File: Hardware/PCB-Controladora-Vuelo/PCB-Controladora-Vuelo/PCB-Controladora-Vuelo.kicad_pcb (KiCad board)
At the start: 2 copper layers, 40 x 90 mm, 14 parts, among them J1 Jumper Serial, J2 CONN, U1 MPU-5060, U2 ESP32-DEVKIT-V1, U3 Nrf24l01, U4 AMS1117-3.3

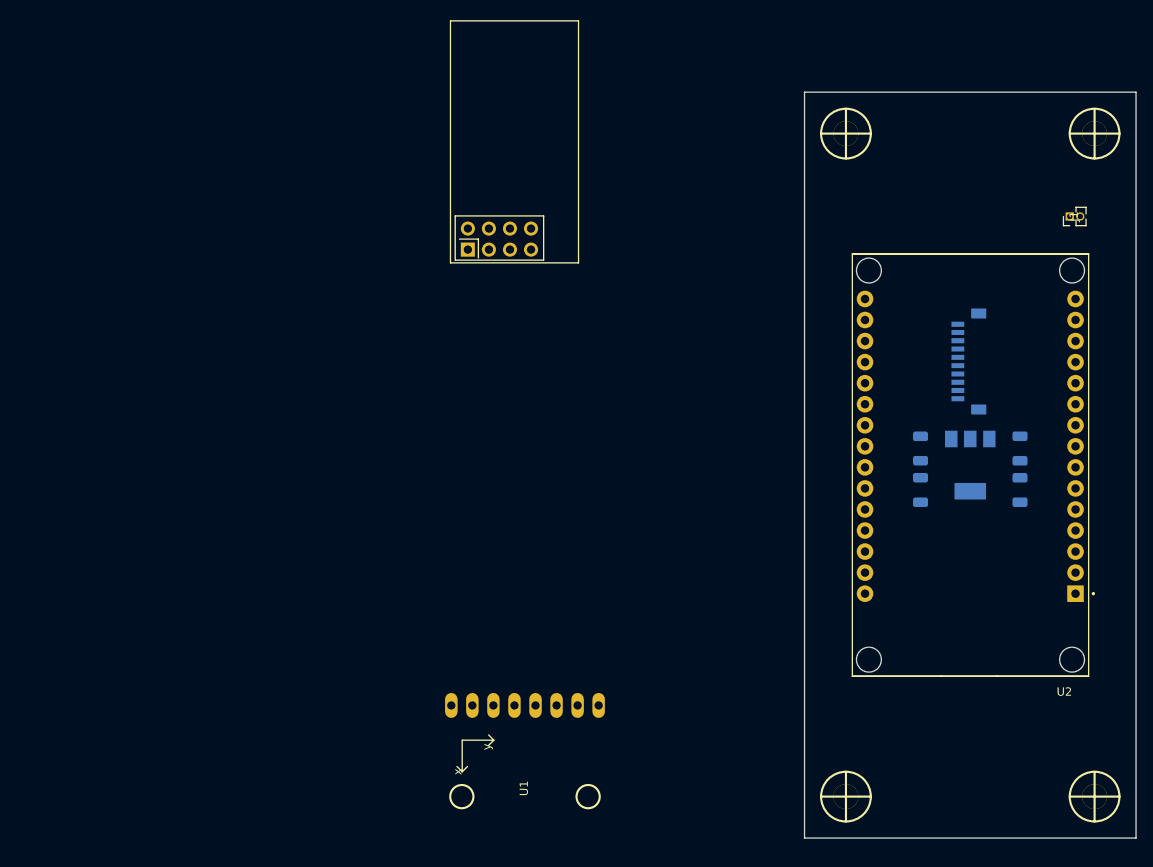
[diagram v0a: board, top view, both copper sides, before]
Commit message: subo cambios hechos en legui solucione mpu y lugar esp32 mal Footprints
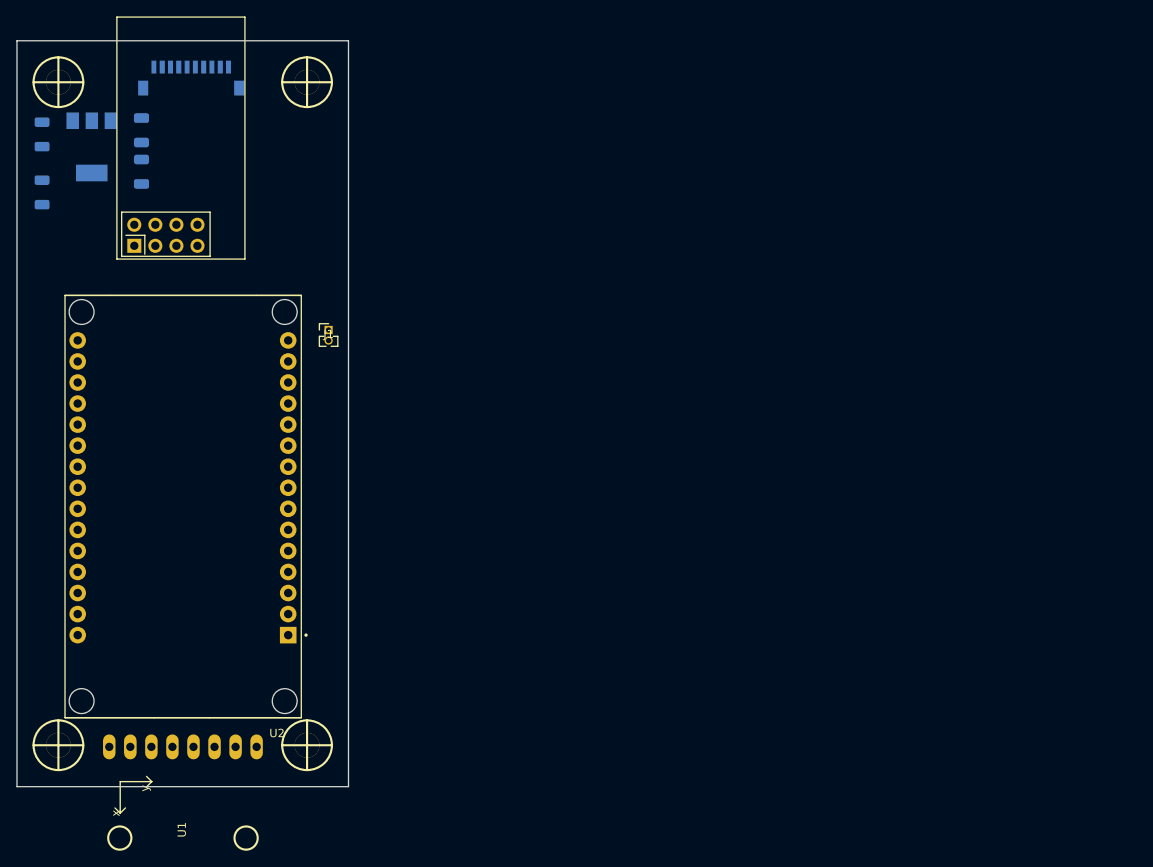
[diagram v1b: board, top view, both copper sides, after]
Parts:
- moved C1 112.7 mm to (129.0, 61.6)
- moved C3 112.7 mm to (129.0, 66.6)
- moved U4 112.7 mm to (123.0, 63.6)
- moved C7 112.6 mm to (117.0, 62.1)
- moved C5 111.9 mm to (117.0, 69.1)
- moved J2 100.6 mm to (135.0, 56.5), turned to 0 degrees
- moved H1 95.2 mm to (119.0, 55.8)
- moved H2 95.2 mm to (149.0, 55.8)
- moved H3 95.2 mm to (149.0, 135.8)
- moved H4 95.2 mm to (119.0, 135.8)
- moved U2 95.1 mm to (134.0, 107.0)
- moved J1 90.5 mm to (151.6, 85.7), turned to 0 degrees
- moved U1 41.6 mm to (142.9, 136.0)
- moved U3 40.3 mm to (128.1, 75.5)

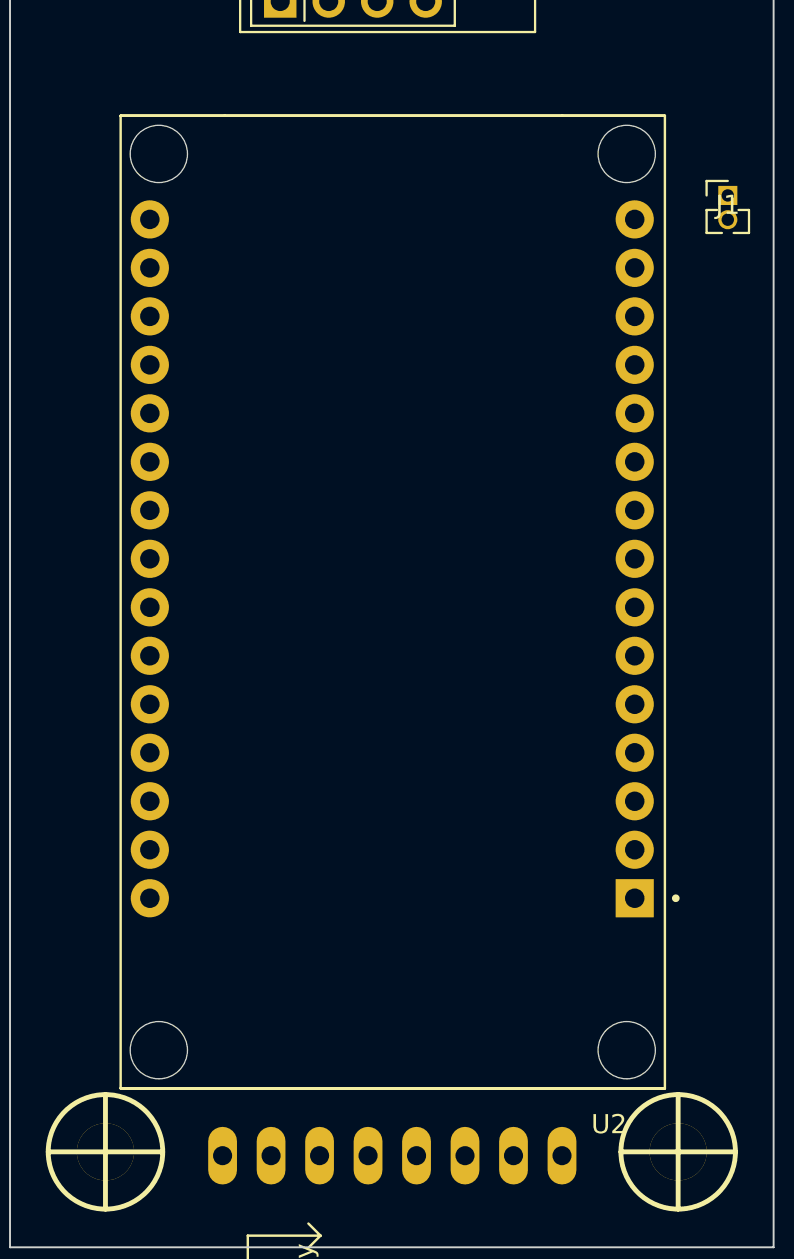
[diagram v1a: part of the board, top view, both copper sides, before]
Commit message: Realice cambios de huella ESP32 y Symbol
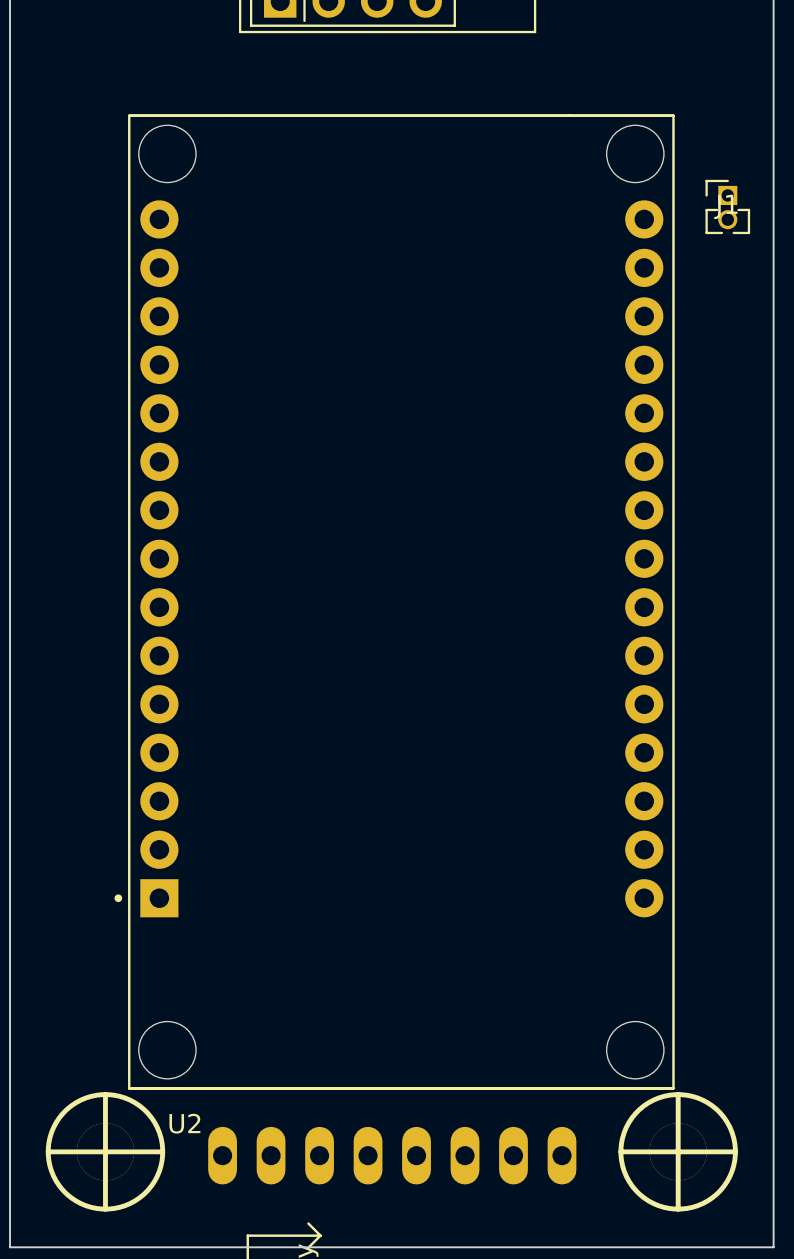
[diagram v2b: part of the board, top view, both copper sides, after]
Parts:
- C1: value 1uF -> 220uF
- C5: value 1uF -> 10uF
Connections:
- J2 pad 1: /NC -> unconnected-(J2-Pad1)
- J2 pad 3: /NC -> unconnected-(J2-Pad3)
- J2 pad 4: /NC -> unconnected-(J2-Pad4)
- J2 pad S1: /NC -> Net-(J2-SHIELD-PadS1)
- J2 pad S2: /NC -> Net-(J2-SHIELD-PadS1)
- U2 pad 1: unconnected-(U2-EN-Pad1) -> /Jumper_Serial
- U2 pad 10: /S2_MOTOR -> unconnected-(U2-D32-Pad10)
- U2 pad 11: /S3_MOTOR -> unconnected-(U2-D35-Pad11)
- U2 pad 12: /S4_MOTOR -> unconnected-(U2-D34-Pad12)
- U2 pad 14: GND -> unconnected-(U2-VP-Pad14)
- U2 pad 15: /Jumper_Serial -> unconnected-(U2-EN-Pad15)
- U2 pad 2: unconnected-(U2-VP-Pad2) -> GND
- U2 pad 4: unconnected-(U2-D34-Pad4) -> /S4_MOTOR
- U2 pad 5: unconnected-(U2-D35-Pad5) -> /S3_MOTOR
- U2 pad 6: unconnected-(U2-D32-Pad6) -> /S2_MOTOR
- U2 pad 7: unconnected-(U2-D33-Pad7) -> /S1_MOTOR
- U2 pad 9: /S1_MOTOR -> unconnected-(U2-D33-Pad9)

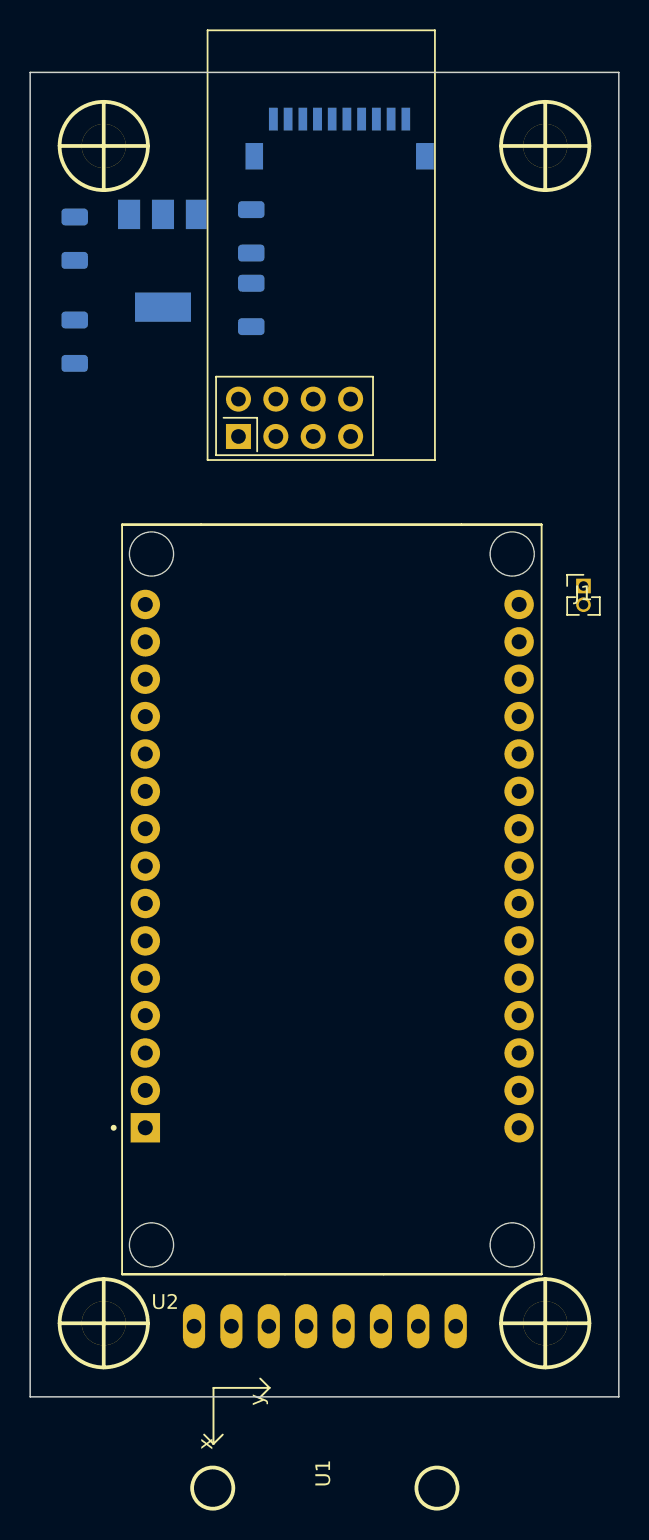
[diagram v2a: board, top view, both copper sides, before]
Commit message: muchos cambios leer saque todos los NC y coloque X ya que al poner etiquetas nc reconoce como que debe haber una conexion entre ellos y nqv tambien digamos que hice una buena 1ra parte de pcb, que se debe corregir y mirar todo mas a detalle , faltan definir unos pines para ver si es necesario para la primera prueba xD
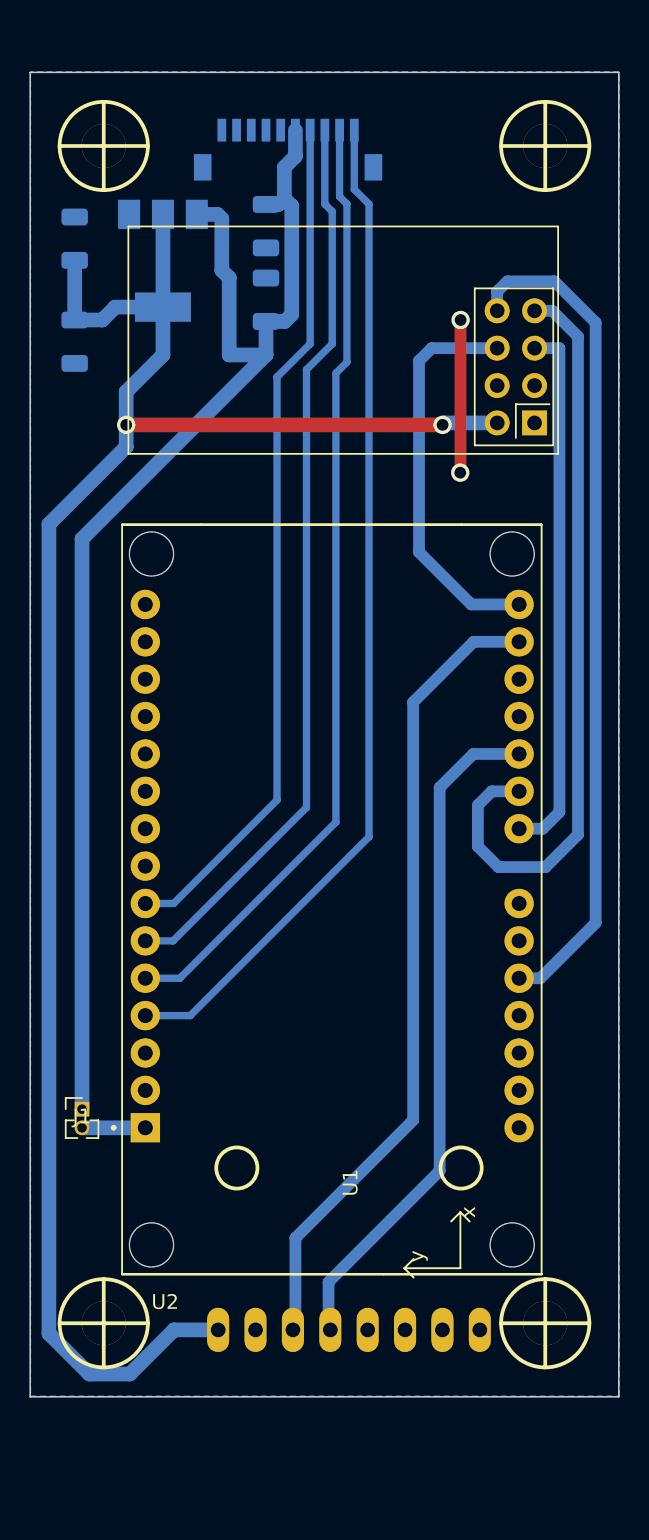
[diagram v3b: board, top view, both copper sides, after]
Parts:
- moved J1 49.2 mm to (117.5, 121.2)
- moved U3 20.1 mm to (148.2, 74.6), turned to 180 degrees
- moved U1 16.1 mm to (126.8, 136.2), turned to 90 degrees
- moved J2 3.58 mm to (131.5, 57.2)
- moved C1 1.06 mm to (130.0, 61.2)
- moved C3 1.06 mm to (130.0, 66.2)
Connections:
- J2 pad S1: Net-(J2-SHIELD-PadS1) -> unconnected-(J2-SHIELD-PadS1)
- J2 pad S2: Net-(J2-SHIELD-PadS1) -> unconnected-(J2-SHIELD-PadS1)
- U1 pad 5: /XDA_MPU6050 -> unconnected-(U1-XDA-Pad5)
- U1 pad 6: /XCL_MPU6050 -> unconnected-(U1-XCL-Pad6)
- U1 pad 7: /AD0_MPU6050 -> unconnected-(U1-ADO-Pad7)
- U1 pad 8: /INT_MPU6050 -> unconnected-(U1-INT-Pad8)
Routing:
- net +3V3: track 0.00 -> 128.8 mm, vias 0 -> 2
- net +5V: track 0.00 -> 88.9 mm
- net /S4_MOTOR: track 0.00 -> 68.7 mm
- net /S3_MOTOR: track 0.00 -> 64.9 mm
- net /S2_MOTOR: track 0.00 -> 61.7 mm
- net /S1_MOTOR: track 0.00 -> 58.3 mm
- net /IRQ_NRF24L01: track 0.00 -> 57.0 mm
- net /SCL_MPU6050: track 0.00 -> 54.9 mm
- net /MISO_NRF24L01: track 0.00 -> 51.8 mm
- net /SDA_MPU6050: track 0.00 -> 46.4 mm
- net /SCK_NRF24L01: track 0.00 -> 36.4 mm
- net /MOSI_NRF24L01: track 0.00 -> 26.9 mm
- net GND: track 0.00 -> 10.4 mm, vias 0 -> 2
- net /Jumper_Serial: track 0.00 -> 4.30 mm
- added copper zone on B.Cu, net GND

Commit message: Trabaje en el PCB corriegindo ordenes faltaria ver si se pueden agregar pines y corregir que no existan riesgo al momento de planchar o por un corto o abrirse el circuito
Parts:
- moved J2 3.23 mm to (134.0, 55.2)
- moved U3 2.55 mm to (145.7, 74.6)
- moved U1 2.47 mm to (125.0, 138.0)
- moved C1 2.38 mm to (132.1, 60.1)
- moved C3 2.38 mm to (132.1, 65.1)
- moved J1 0.62 mm to (118.1, 121.1)
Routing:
- net +3V3: track 128.8 -> 139.0 mm
- net GND: track 10.4 -> 19.1 mm
- net /S4_MOTOR: track 68.7 -> 72.7 mm
- net /S1_MOTOR: track 58.3 -> 62.2 mm
- net /S3_MOTOR: track 64.9 -> 68.7 mm
- net /S2_MOTOR: track 61.7 -> 65.3 mm
- net +5V: track 88.9 -> 85.9 mm
- net /IRQ_NRF24L01: track 57.0 -> 59.7 mm
- net /SCL_MPU6050: track 54.9 -> 57.5 mm
- net /SDA_MPU6050: track 46.4 -> 48.8 mm
- net /MISO_NRF24L01: track 51.8 -> 53.7 mm
- net /MOSI_NRF24L01: track 26.9 -> 25.9 mm
- net /SCK_NRF24L01: track 36.4 -> 37.0 mm
- net /Jumper_Serial: track 4.30 -> 3.76 mm

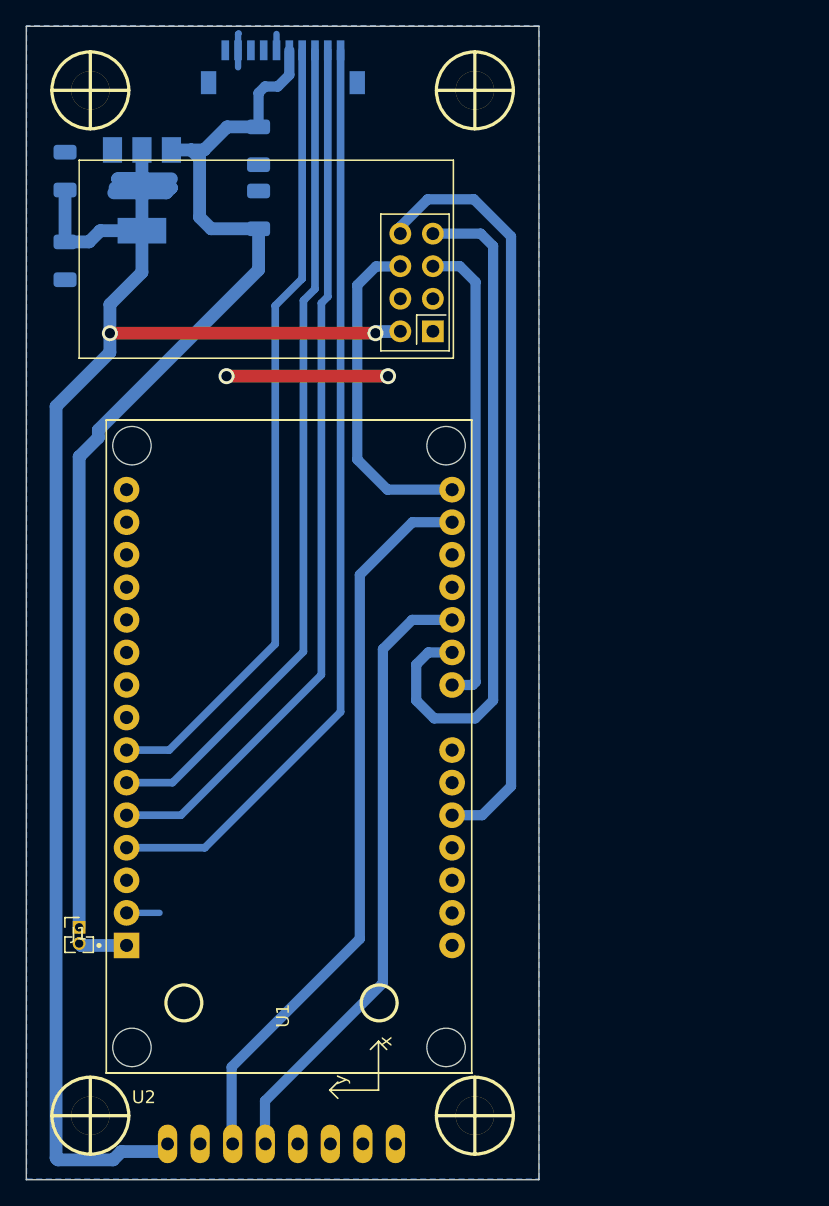
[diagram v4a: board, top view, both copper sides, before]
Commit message: Hice una mejora con un solo puente de  pista 3,3v para transeptor en donde existen riesgos pero mañana trato d mejorar y chequear pines asi se mergea
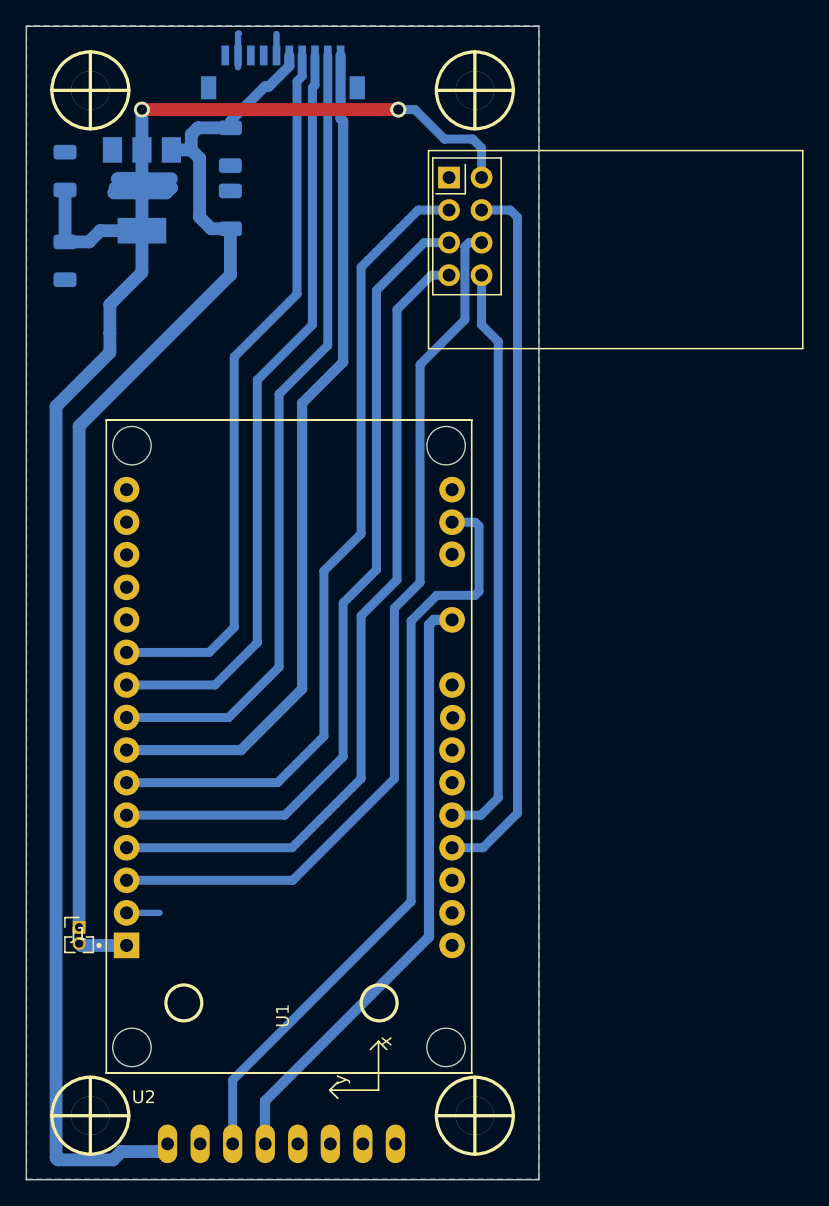
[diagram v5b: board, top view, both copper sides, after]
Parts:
- moved U3 12.1 mm to (147.0, 62.6), turned to 0 degrees
- moved C1 2.20 mm to (129.9, 60.2)
- moved C3 2.20 mm to (129.9, 65.1)
- moved J2 0.40 mm to (134.0, 55.6)
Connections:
- U2 pad 10: unconnected-(U2-D32-Pad10) -> /S1_MOTOR
- U2 pad 16: /MOSI_NRF24L01 -> unconnected-(U2-D23-Pad16)
- U2 pad 22: /SCK_NRF24L01 -> unconnected-(U2-D18-Pad22)
- U2 pad 27: unconnected-(U2-D15-Pad27) -> /CSN_NRF24L01
- U2 pad 3: unconnected-(U2-D13-Pad3) -> /MOSI_NRF24L01
- U2 pad 4: /S4_MOTOR -> /MISO_NRF24L01
- U2 pad 5: /S3_MOTOR -> /SCK_NRF24L01
- U2 pad 6: /S2_MOTOR -> /CE_NRF24L01
- U2 pad 7: /S1_MOTOR -> /S4_MOTOR
- U2 pad 8: unconnected-(U2-D25-Pad8) -> /S3_MOTOR
- U2 pad 9: unconnected-(U2-D33-Pad9) -> /S2_MOTOR
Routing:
- net /CE_NRF24L01: track 0.00 -> 63.4 mm
- net /CSN_NRF24L01: track 0.00 -> 55.7 mm
- net /MOSI_NRF24L01: track 25.9 -> 69.4 mm
- net /SCK_NRF24L01: track 37.0 -> 63.5 mm
- net /IRQ_NRF24L01: track 59.7 -> 45.5 mm
- net GND: track 19.1 -> 6.92 mm, vias 2 -> 0
- net +3V3: track 139.0 -> 149.5 mm
- net /MISO_NRF24L01: track 53.7 -> 63.5 mm
- net /S4_MOTOR: track 72.7 -> 66.5 mm
- net /S1_MOTOR: track 62.2 -> 56.0 mm
- net /S2_MOTOR: track 65.3 -> 59.3 mm
- net /S3_MOTOR: track 68.7 -> 62.8 mm
- net +5V: track 85.9 -> 81.4 mm
- net /SCL_MPU6050: track 57.5 -> 60.1 mm
- net /SDA_MPU6050: track 48.8 -> 47.8 mm
